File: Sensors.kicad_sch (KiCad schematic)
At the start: 14 parts, among them U3 INA226

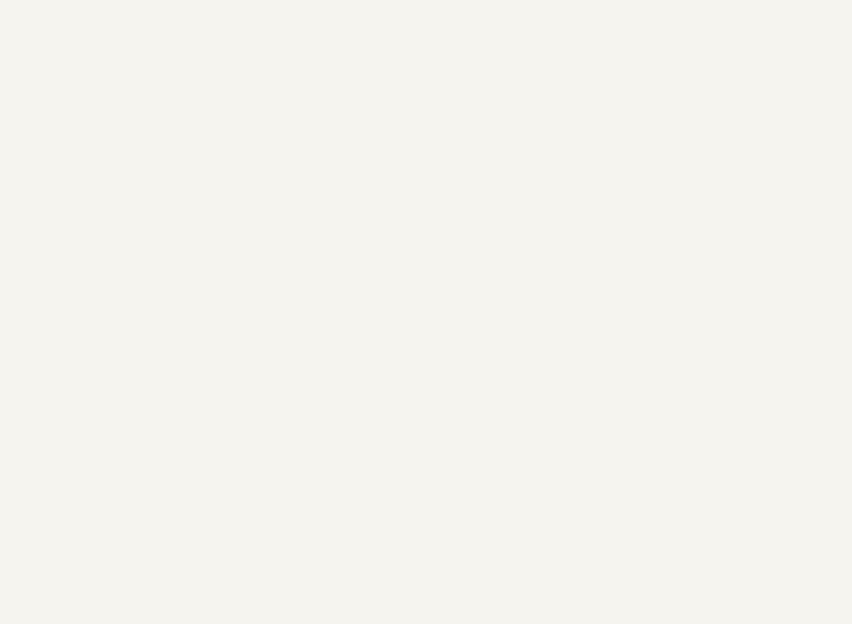
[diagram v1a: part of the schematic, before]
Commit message: schematic for OP amp based current sensor
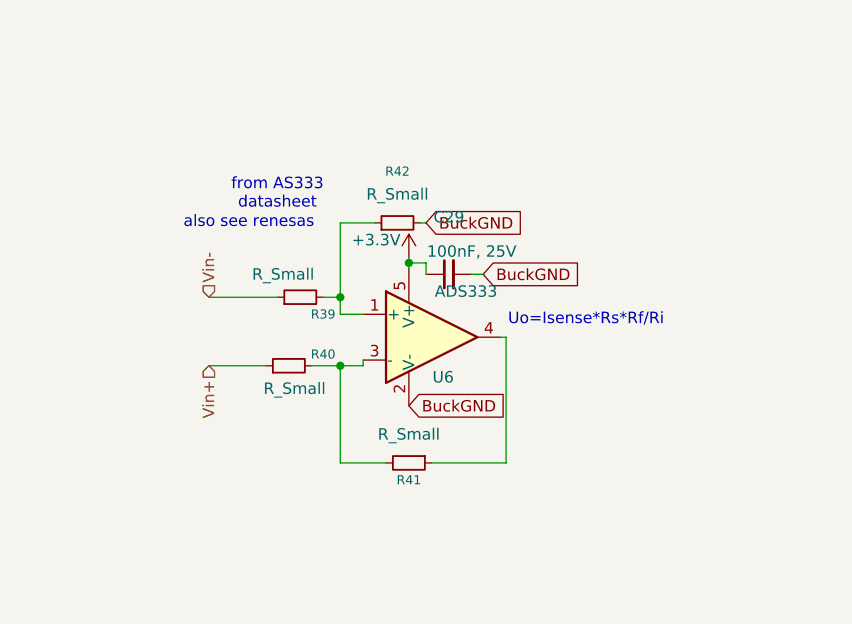
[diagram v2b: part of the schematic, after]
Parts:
- added C29: 100nF, 25V, Capacitor_SMD:C_0805_2012Metric, symbol Device:C_Small
- added R39, R40, R41, R42: R_Small, Resistor_SMD:R_0805_2012Metric, symbol Device:R_Small
- added U6: ADS333, Package_TO_SOT_SMD:SOT-353_SC-70-5, symbol Amplifier_Operational:TLV172IDCK
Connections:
- net +3.3V: now also C29.1, U6.5 (V+)
- net Vin+: now also R40.1
- net Vin-: now also R39.1
- new net: R39.2, R42.1, U6.1 (+)
- new net: R41.1, U6.4
- new net: R40.2, R41.2, U6.3 (-)
- new net BuckGND: C29.2, R42.2, U6.2 (V-)
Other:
- note added: "Uo=Isense*Rs*Rf/Ri"
- note added: "also see renesas"
- note added: "from AS333 datasheet"

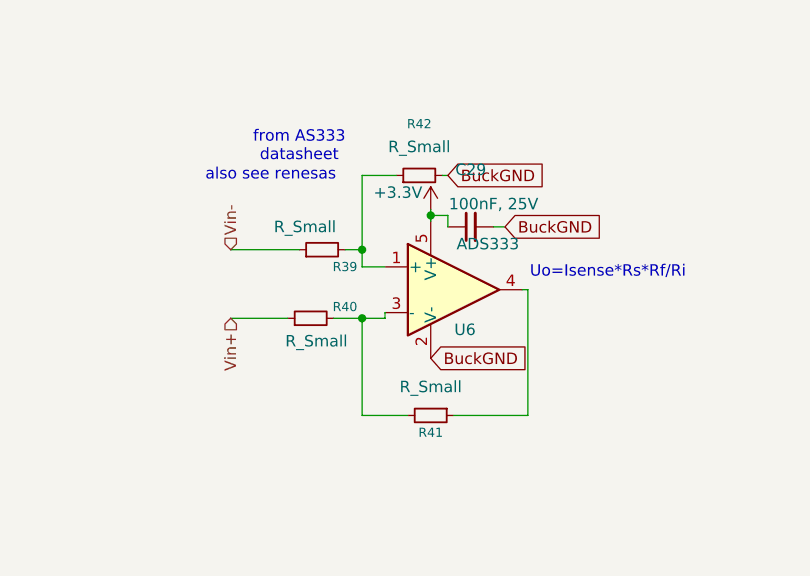
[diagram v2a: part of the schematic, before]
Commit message: dnp new current sense circuit
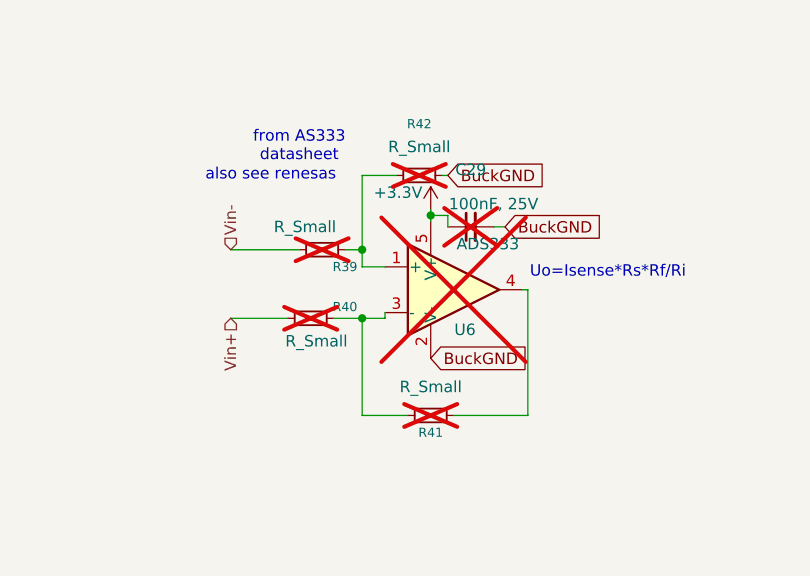
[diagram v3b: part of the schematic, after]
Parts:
- C29, R39, R40, R41, R42, U6: now not fitted
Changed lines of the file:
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@@
 		(exclude_from_sim no)
 		(in_bom yes)
-		(on_board yes)
-		(dnp no)
+		(on_board no)
+		(dnp yes)
 		(property "Reference" "R39"
 			(at 127.635 122.555 90)
@@
 		(exclude_from_sim no)
 		(in_bom yes)
-		(on_board yes)
-		(dnp no)
+		(on_board no)
+		(dnp yes)
 		(fields_autoplaced yes)
 		(property "Reference" "R42"
@@
 		(exclude_from_sim no)
 		(in_bom yes)
-		(on_board yes)
-		(dnp no)
+		(on_board no)
+		(dnp yes)
 		(property "Reference" "R41"
 			(at 137.16 140.97 90)
@@
 		(exclude_from_sim no)
 		(in_bom yes)
-		(on_board yes)
-		(dnp no)
+		(on_board no)
+		(dnp yes)
 		(property "Reference" "C29"
 			(at 141.6113 111.76 90)
@@
 		(exclude_from_sim no)
 		(in_bom yes)
-		(on_board yes)
-		(dnp no)
+		(on_board no)
+		(dnp yes)
 		(property "Reference" "R40"
 			(at 127.635 127 90)
@@
 		(exclude_from_sim no)
 		(in_bom yes)
-		(on_board yes)
-		(dnp no)
+		(on_board no)
+		(dnp yes)
 		(property "Reference" "U6"
 			(at 140.97 129.54 0)

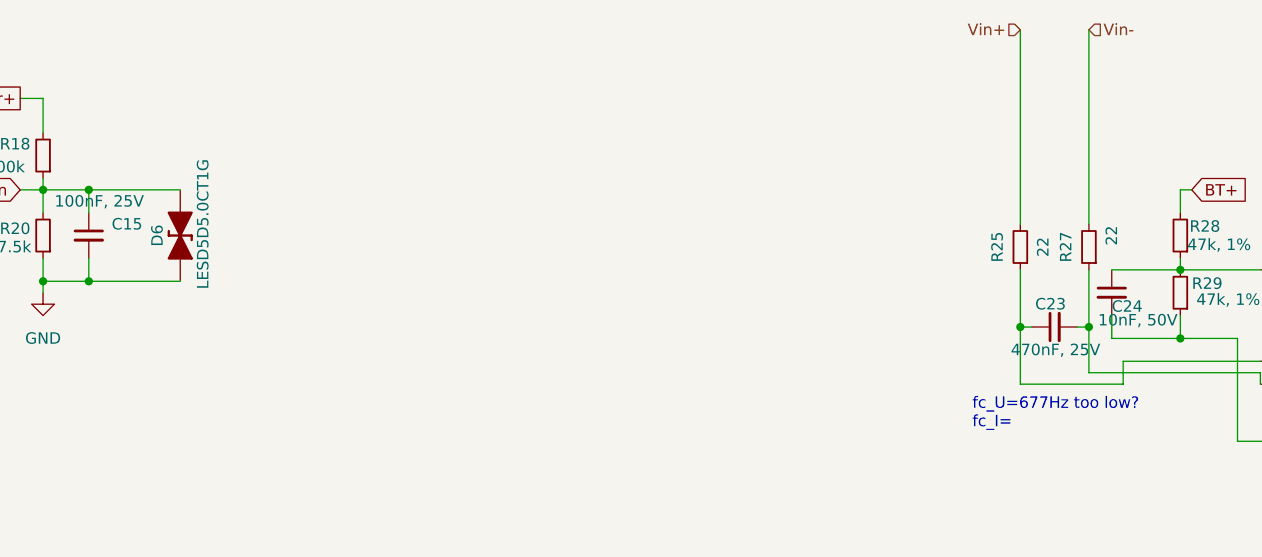
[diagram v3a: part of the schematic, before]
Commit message: bom optimization
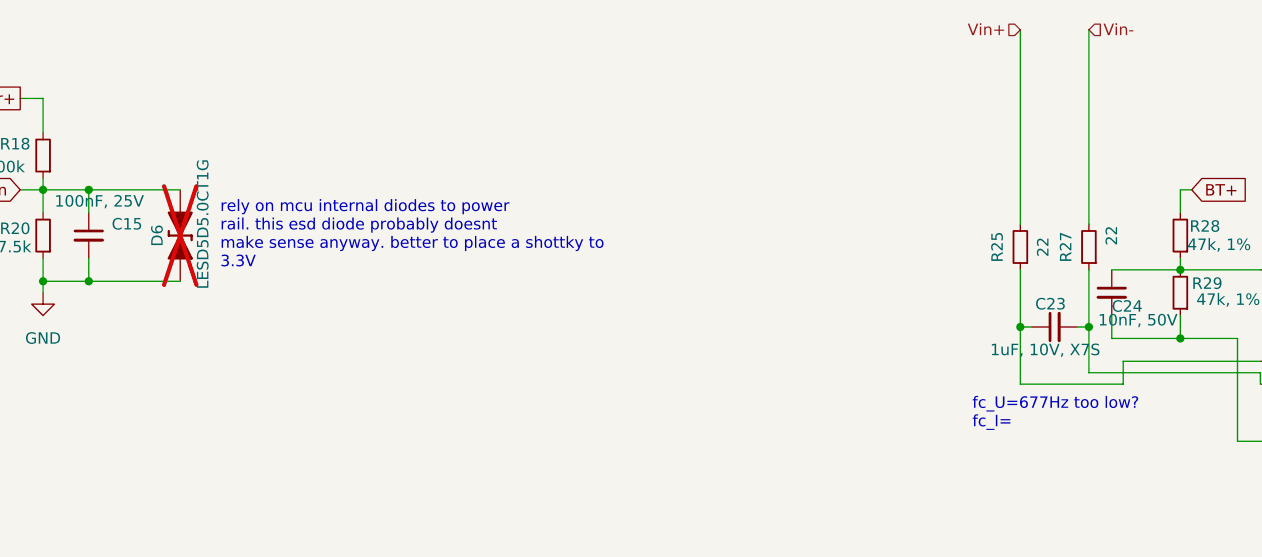
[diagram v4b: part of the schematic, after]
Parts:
- C23: value 470nF, 25V -> 1uF, 10V, X7S
- D6: now not fitted; now left out of the parts list
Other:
- note added: "rely on mcu internal diodes to power rail. this esd diode probably doesnt make sense anyway. better to place a shottky to 3.3V"
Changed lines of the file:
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@@
 	(generator_version "9.0")
 	(paper "A4")
+	(text "rely on mcu internal diodes to power\nrail. this esd diode probably doesnt\nmake sense anyway. better to place a shottky to\n3.3V"
+		(exclude_from_sim no)
+		(at 90.805 57.785 0)
+		(effects
+			(font
+				(size 1.27 1.27)
+			)
+			(justify left)
+		)
+	)
 	(text "from AS333\ndatasheet"
 		(exclude_from_sim no)
@@
 			)
 		)
-		(property "Value" "470nF, 25V"
+		(property "Value" "1uF, 10V, X7S"
 			(at 188.595 70.485 90)
 			(effects
@@
 		(unit 1)
 		(exclude_from_sim no)
-		(in_bom yes)
+		(in_bom no)
 		(on_board yes)
-		(dnp no)
+		(dnp yes)
 		(property "Reference" "D6"
 			(at 83.82 57.785 0)

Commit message: cleanup schematics
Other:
- note added: "new INA226 replacement circuit (bi-directional, cheaper)"
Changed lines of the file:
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@@
+		)
+	)
+	(text "new INA226 replacement\ncircuit (bi-directional, cheaper)"
+		(exclude_from_sim no)
+		(at 132.715 100.33 0)
+		(effects
+			(font
+				(size 1.27 1.27)
+			)
 		)
 	)

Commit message: bom
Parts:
- C15, C25: value 100nF, 25V -> 100nF, X7R, 25V; MPN 100nF, 25V -> 100nF, X7R, 25V
- C23: Digikey (none) -> CL21B105KAFNNNE; MPN 470nF, 25V -> 1uF, 10V, X7S
- C24: value 10nF, 50V -> 10nF, 100V; Digikey (none) -> 0805B103K101CT; MPN 10nF, 50V -> 10nF, 100V
- R28, R29: MPN 47k 1% -> 47k, 1%
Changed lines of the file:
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@@
 			)
 		)
-		(property "MPN" "470nF, 25V"
+		(property "MPN" "1uF, 10V, X7S"
 			(at 183.515 67.945 0)
 			(effects
@@
 			)
 		)
-		(property "Digikey" ""
+		(property "Digikey" "CL21B105KAFNNNE"
 			(at 183.515 67.945 0)
 			(effects
@@
 			)
 		)
-		(property "MPN" "47k 1%"
+		(property "MPN" "47k, 1%"
 			(at 197.485 57.785 0)
 			(effects
@@
 			)
 		)
-		(property "Value" "100nF, 25V"
+		(property "Value" "100nF, X7R, 25V"
 			(at 224.155 53.975 90)
 			(effects
@@
 			)
 		)
-		(property "MPN" "100nF, 25V"
+		(property "MPN" "100nF, X7R, 25V"
 			(at 221.615 56.515 0)
 			(effects
@@
 			)
 		)
-		(property "Value" "100nF, 25V"
+		(property "Value" "100nF, X7R, 25V"
 			(at 72.39 53.975 0)
 			(effects
@@
 			)
 		)
-		(property "MPN" "100nF, 25V"
+		(property "MPN" "100nF, X7R, 25V"
 			(at 76.2 57.785 0)
 			(effects
@@
 			)
 		)
-		(property "Value" "10nF, 50V"
+		(property "Value" "10nF, 100V"
 			(at 188.341 67.183 0)
 			(effects
@@
 			)
 		)
-		(property "MPN" "10nF, 50V"
+		(property "MPN" "10nF, 100V"
 			(at 189.865 64.135 0)
 			(effects
@@
 			)
 		)
-		(property "Digikey" ""
+		(property "Digikey" "0805B103K101CT"
 			(at 189.865 64.135 0)
 			(effects
@@
 			)
 		)
-		(property "MPN" "47k 1%"
+		(property "MPN" "47k, 1%"
 			(at 197.485 64.135 0)
 			(effects

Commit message: opa current sense
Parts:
- added C26: 1uF, Capacitor_SMD:C_0805_2012Metric, symbol Device:C_Small
- added R30: 100k, Resistor_SMD:R_0805_2012Metric, symbol Device:R_Small
- R39, R40: value R_Small -> 1k
- R41: value R_Small -> 75k
- R42: value R_Small -> 100k
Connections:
- net +3.3V: now also R42.2
- net BuckGND: now also R30.1; no longer R42.2
- net at R39.2, R42.1, U6.1 (+): now also C26.2, R30.2
- net at R40.2, R41.2, U6.3 (-): now also C26.1
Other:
- note added: "c is filter and transient suppressor"
- moved on the sheet: C29, R39, R40, R42

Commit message: pre-opa
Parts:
- removed R30: 100k, Resistor_SMD:R_0805_2012Metric, symbol Device:R_Small
- added C32: 100pF, Capacitor_SMD:C_0805_2012Metric, symbol Device:C_Small
- C15: value 100nF, X7R, 25V -> 10nF, 100V; MPN 100nF, X7R, 25V -> 10nF, 100V
- C26: value 1uF -> 100nF; Desc bypass -> (none); MPN 100nF, 25V -> (none)
- R16: Desc (none) -> NTC
- R42: value 100k -> 150k
- U6: value ADS333 -> AS333
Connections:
- net at R39.2, R42.1, U6.1 (+): now also C26.1; no longer C26.2
- net at R41.1, U6.4: now also C32.1
- net at R40.2, R41.2, U6.3 (-): now also C26.2, C32.2; no longer C26.1
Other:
- note added: "C26 (optional) - transient suppressor"
- note added: "RC is filter and transient suppressor"
- note added: "TODO: use GND here instead of BuckGND"
- note added: "circuitjs"
- note added: "cjs2"
- note added: "f_c=1/(2pi*R20*C15) f_c=221Hz t_r=R*C*2.2 (10-90%) t_r=1.6ms"
- note added: "fc_U=677Hz too low? fc_I=3.6kHz"
- note added: "filtered voltage divider fc~=(R1+R2)/(2pi*R1*R2*C)"
- note added: "input filtering is necessary to filter out PWM signal 5kHz (-3db) should be fine"
- note removed: "c is filter and transient suppressor"
- note removed: "f_c=1/(2pi*R20*C15) f_c=221Hz"
- note removed: "fc_U=677Hz too low? fc_I="
- moved on the sheet: R40
